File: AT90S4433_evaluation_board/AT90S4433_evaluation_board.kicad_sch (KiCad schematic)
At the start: 29 parts, among them SW1 USR_BTN, Y1 Crystal_Small

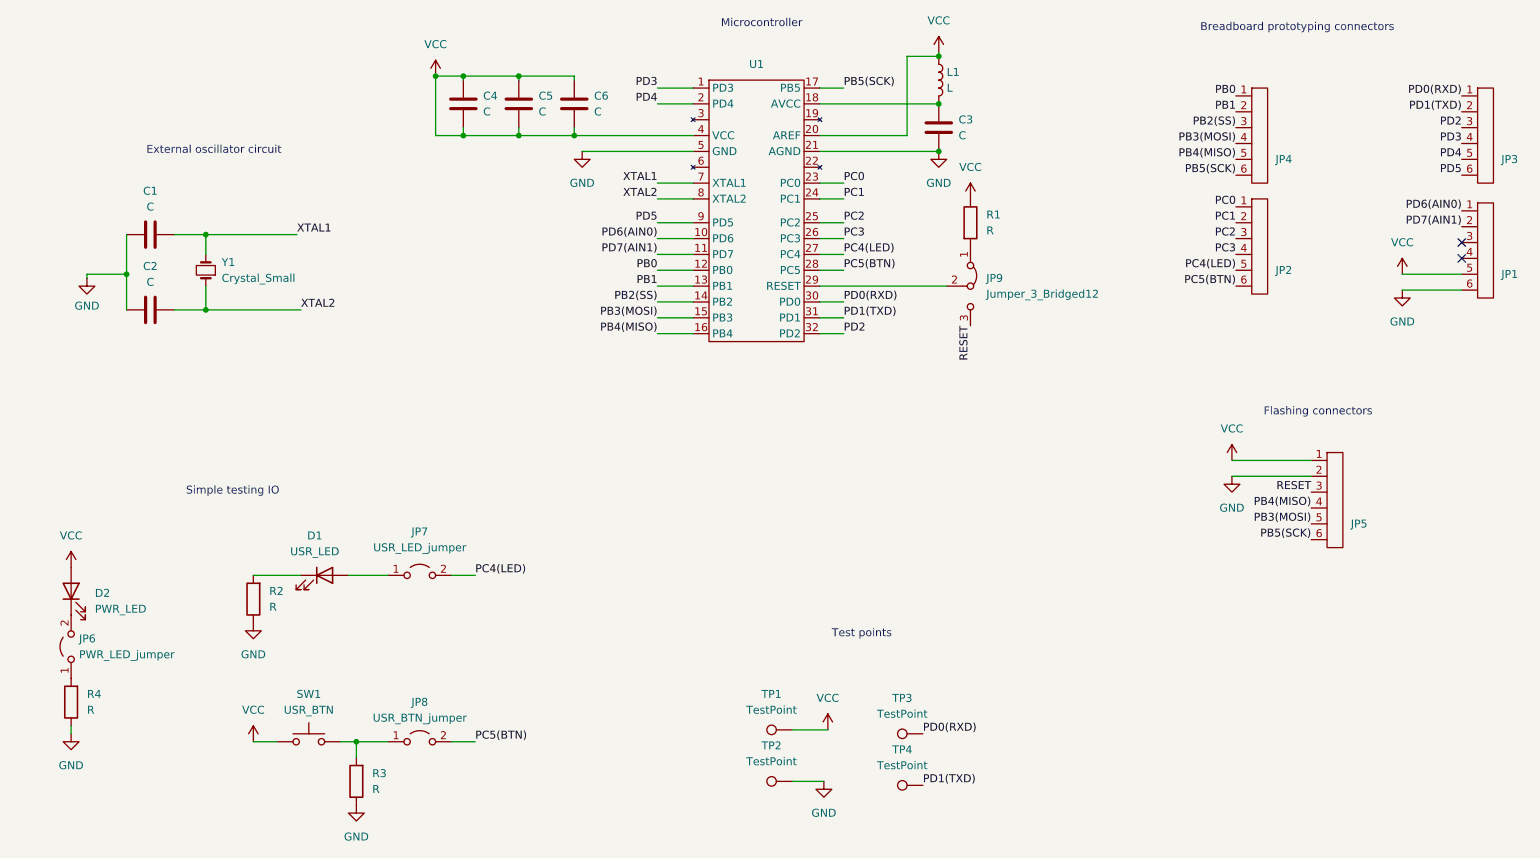
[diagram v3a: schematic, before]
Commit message: footprints corrections, key components initial layout
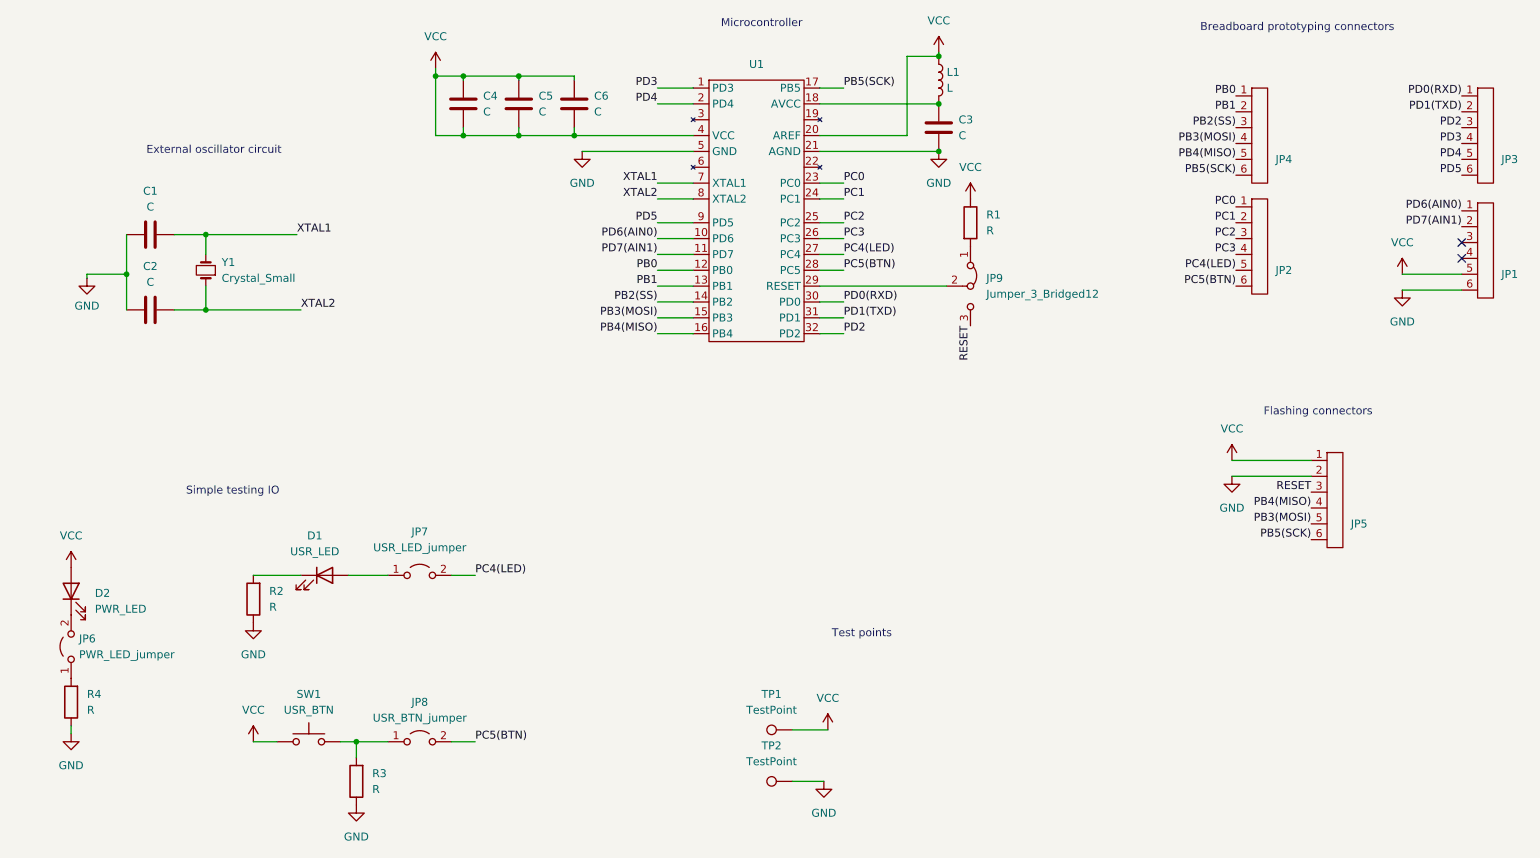
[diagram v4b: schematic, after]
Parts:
- removed TP3, TP4: TestPoint, TestPoint:TestPoint_THTPad_D2.0mm_Drill1.0mm, symbol Connector:TestPoint
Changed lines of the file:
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@@
+    (stroke (width 0) (type default))
+  )
+  (wire (pts (xy 84.455 38.735) (xy 84.455 40.005))
     (stroke (width 0) (type default))
   )
@@
     (effects (font (size 1.27 1.27)) (justify left bottom))
   )
-  (label "PD1(TXD)" (at 162.56 153.67 0) (fields_autoplaced)
-    (effects (font (size 1.27 1.27)) (justify left bottom))
-  )
   (label "PB3(MOSI)" (at 212.725 50.8 180) (fields_autoplaced)
     (effects (font (size 1.27 1.27)) (justify right bottom))
@@
   (label "PD5" (at 120.015 63.5 180) (fields_autoplaced)
     (effects (font (size 1.27 1.27)) (justify right bottom))
-  )
-  (label "PD0(RXD)" (at 162.56 145.415 0) (fields_autoplaced)
-    (effects (font (size 1.27 1.27)) (justify left bottom))
   )
   (label "PC3" (at 149.86 66.04 0) (fields_autoplaced)
@@
     )
   )
-  (symbol (lib_id "power:VCC") (at 84.455 40.005 0) (unit 1)
-    (in_bom yes) (on_board yes) (dnp no) (fields_autoplaced)
-    (property "Reference" "#PWR02" (at 84.455 43.815 0)
-      (effects (font (size 1.27 1.27)) hide)
-    )
-    (property "Value" "VCC" (at 84.455 34.925 0)
-      (effects (font (size 1.27 1.27)))
-    )
-    (property "Footprint" "" (at 84.455 40.005 0)
-      (effects (font (size 1.27 1.27)) hide)
-    )
-    (property "Datasheet" "" (at 84.455 40.005 0)
+  (symbol (lib_id "power:VCC") (at 84.455 38.735 0) (unit 1)
+    (in_bom yes) (on_board yes) (dnp no) (fields_autoplaced)
+    (property "Reference" "#PWR02" (at 84.455 42.545 0)
+      (effects (font (size 1.27 1.27)) hide)
+    )
+    (property "Value" "VCC" (at 84.455 33.655 0)
+      (effects (font (size 1.27 1.27)))
+    )
+    (property "Footprint" "" (at 84.455 38.735 0)
+      (effects (font (size 1.27 1.27)) hide)
+    )
+    (property "Datasheet" "" (at 84.455 38.735 0)
       (effects (font (size 1.27 1.27)) hide)
     )
@@
     )
   )
-  (symbol (lib_id "Connector:TestPoint") (at 162.56 145.415 90) (unit 1)
-    (in_bom yes) (on_board yes) (dnp no) (fields_autoplaced)
-    (property "Reference" "TP3" (at 159.258 139.7 90)
-      (effects (font (size 1.27 1.27)))
-    )
-    (property "Value" "TestPoint" (at 159.258 142.24 90)
-      (effects (font (size 1.27 1.27)))
-    )
-    (property "Footprint" "TestPoint:TestPoint_THTPad_D2.0mm_Drill1.0mm" (at 162.56 140.335 0)
-      (effects (font (size 1.27 1.27)) hide)
-    )
-    (property "Datasheet" "~" (at 162.56 140.335 0)
-      (effects (font (size 1.27 1.27)) hide)
-    )
-    (pin "1")
-    (instances
-      (project "AT90S4433_evaluation_board"
-        (path "/7ff8dc4c-cb91-450f-a04d-1629054ff54a"
-          (reference "TP3") (unit 1)
-        )
-      )
-    )
-  )
   (symbol (lib_id "Device:R") (at 170.18 63.5 0) (unit 1)
     (in_bom yes) (on_board yes) (dnp no) (fields_autoplaced)
@@
         )
       )
-    )
-  )
-  (symbol (lib_id "Connector:TestPoint") (at 162.56 153.67 90) (unit 1)
-    (in_bom yes) (on_board yes) (dnp no) (fields_autoplaced)
-    (property "Reference" "TP4" (at 159.258 147.955 90)
-      (effects (font (size 1.27 1.27)))
-    )
-    (property "Value" "TestPoint" (at 159.258 150.495 90)
-      (effects (font (size 1.27 1.27)))
-    )
-    (property "Footprint" "TestPoint:TestPoint_THTPad_D2.0mm_Drill1.0mm" (at 162.56 148.59 0)
-      (effects (font (size 1.27 1.27)) hide)
-    )
-    (property "Datasheet" "~" (at 162.56 148.59 0)
-      (effects (font (size 1.27 1.27)) hide)
-    )
-    (pin "1")
-    (instances
-      (project "AT90S4433_evaluation_board"
-        (path "/7ff8dc4c-cb91-450f-a04d-1629054ff54a"
-          (reference "TP4") (unit 1)
-        )
-      )

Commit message: initial footprints for all components, modified layout
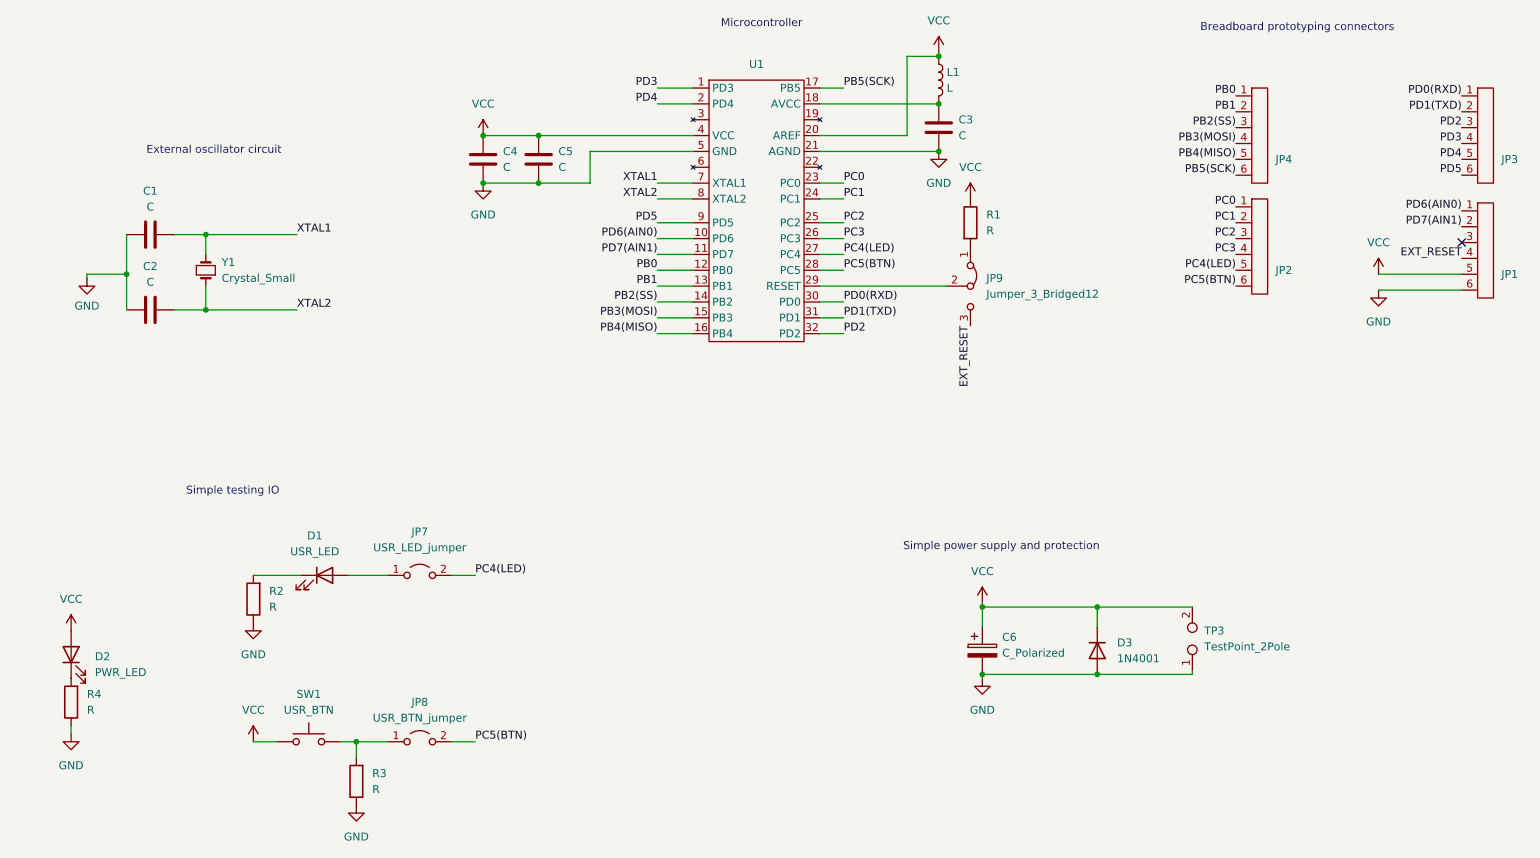
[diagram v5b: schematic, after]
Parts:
- removed C6: C, symbol Device:C
- removed JP5: ~, project_lib_footprints:breadboard_pins, symbol project_lib:breadboard_pins
- removed JP6: PWR_LED_jumper, project_lib_footprints:2_pin_jumper_socket, symbol Jumper:Jumper_2_Open
- removed TP1: TestPoint, TestPoint:TestPoint_THTPad_D2.0mm_Drill1.0mm, symbol Connector:TestPoint
- removed TP2: TestPoint, TestPoint:TestPoint_THTPad_2.0x2.0mm_Drill1.0mm, symbol Connector:TestPoint
- added C6: C_Polarized, Capacitor_THT:CP_Radial_D5.0mm_P2.50mm, symbol Device:C_Polarized
- added D3: 1N4001, Diode_THT:D_DO-41_SOD81_P10.16mm_Horizontal, symbol Diode:1N4001
- added TP3: TestPoint_2Pole, Connector_PinSocket_2.54mm:PinSocket_1x02_P2.54mm_Vertical, symbol Connector:TestPoint_2Pole
- C1, C2, C3, C4, C5: footprint (none) -> Capacitor_SMD:C_0805_2012Metric
- D1, D2: footprint (none) -> LED_SMD:LED_1206_3216Metric
- L1: footprint (none) -> Inductor_SMD:L_0805_2012Metric
- R1, R2, R3, R4: footprint (none) -> Resistor_SMD:R_0805_2012Metric
- SW1: footprint (none) -> Button_Switch_THT:SW_Tactile_Straight_KSA0Axx1LFTR
- Y1: footprint (none) -> Crystal:Crystal_HC18-U_Vertical
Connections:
- net RESET is gone; now on net EXT_RESET: JP9.3 (B)
- net GND: now also C4.1, C5.1, C6.2, D3.2 (A), TP3.1
- net VCC: now also C6.1, D3.1 (K), TP3.2; no longer C4.1, C5.1
- net EXT_RESET: now reaches JP1.4
- net at R4.2: now also D2.1 (K)
- no-connect marks 2 -> 1
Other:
- note added: "Simple power supply and protection"
- note removed: "Flashing connectors"
- note removed: "Test points"
- moved on the sheet: D2

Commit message: first routes
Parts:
- TP3: footprint Connector_PinSocket_2.54mm:PinSocket_1x02_P2.54mm_Vertical -> project_lib_footprints:Power_socker
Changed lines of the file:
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@@
       (effects (font (size 1.27 1.27)) (justify right))
     )
-    (property "Footprint" "Connector_PinSocket_2.54mm:PinSocket_1x02_P2.54mm_Vertical" (at 205.74 130.175 0)
+    (property "Footprint" "project_lib_footprints:Power_socker" (at 205.74 130.175 0)
       (effects (font (size 1.27 1.27)) hide)
     )
